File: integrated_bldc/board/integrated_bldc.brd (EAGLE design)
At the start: 26 x 23 mm, 68 parts, among them J2 PRG

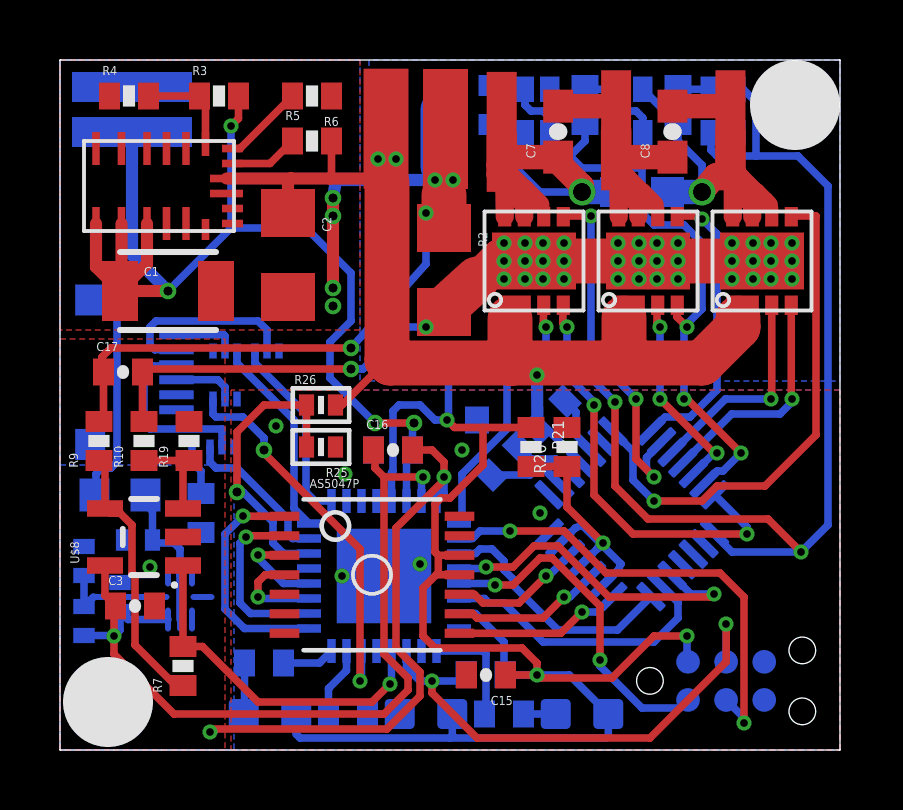
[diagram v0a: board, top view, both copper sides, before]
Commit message: Integrated BLDC is clean from Bay Area Circuits DFM check.
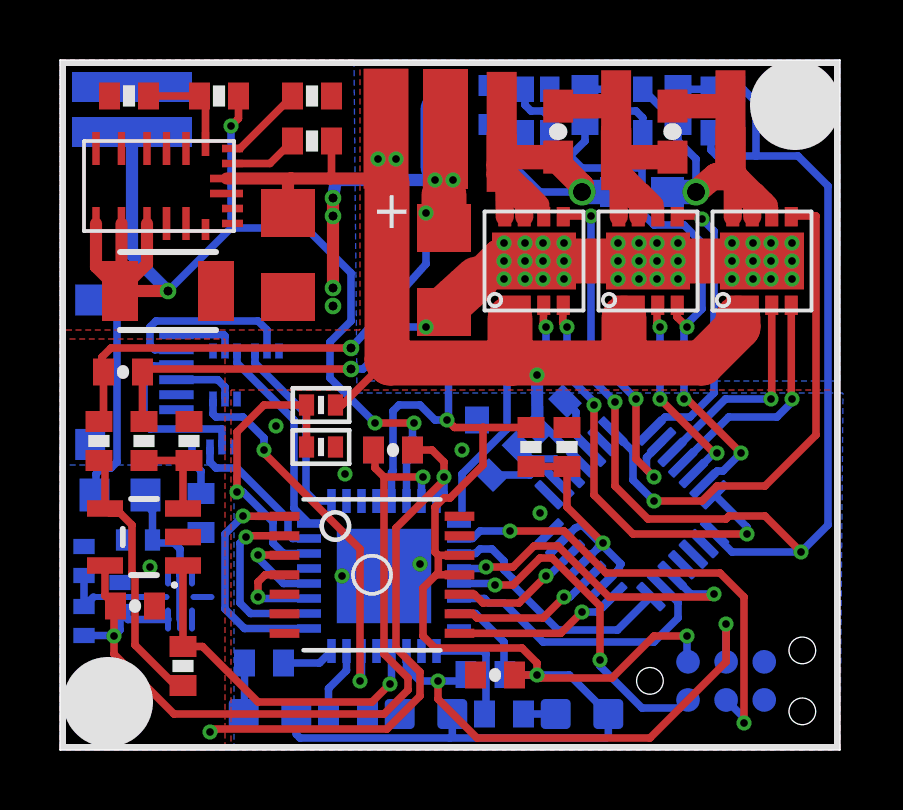
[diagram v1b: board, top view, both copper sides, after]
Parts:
- R14, R15, R8: value 220 -> 220R
- R2: value 0.01 -> 0R01
- moved C15 0.30 mm to (14.5, 2.50)
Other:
- board text added: "+"
- board text added: "-"
- board text added: "RX"
- board text added: "SCL"
- board text added: "SDA"
- board text added: "TX"

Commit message: Finished Dev board layout. Added stop mask to vias. Corrected some component values based on part order.
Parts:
- added U$16: (no value), modular_robotics:INFO
- D12: value GREEN -> WHITE
- R26: value 40k -> 39k
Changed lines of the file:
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@@
 <setting verticaltext="up"/>
 </settings>
-<grid distance="0.1" unitdist="mm" unit="mm" style="dots" multiple="1" display="yes" altdistance="0.005" altunitdist="mm" altunit="mm"/>
+<grid distance="0.1" unitdist="mm" unit="mm" style="dots" multiple="5" display="yes" altdistance="0.005" altunitdist="mm" altunit="mm"/>
 <layers>
 <layer number="1" name="Top" color="4" fill="1" visible="no" active="yes"/>
@@
 <layer number="24" name="bOrigins" color="15" fill="1" visible="yes" active="yes"/>
 <layer number="25" name="tNames" color="7" fill="1" visible="no" active="yes"/>
-<layer number="26" name="bNames" color="7" fill="1" visible="no" active="yes"/>
+<layer number="26" name="bNames" color="7" fill="1" visible="yes" active="yes"/>
 <layer number="27" name="tValues" color="7" fill="1" visible="no" active="yes"/>
-<layer number="28" name="bValues" color="7" fill="1" visible="no" active="yes"/>
+<layer number="28" name="bValues" color="7" fill="1" visible="yes" active="yes"/>
 <layer number="29" name="tStop" color="7" fill="3" visible="no" active="yes"/>
 <layer number="30" name="bStop" color="7" fill="6" visible="yes" active="yes"/>
@@
 <layer number="50" name="dxf" color="7" fill="1" visible="no" active="no"/>
 <layer number="51" name="tDocu" color="7" fill="1" visible="no" active="yes"/>
-<layer number="52" name="bDocu" color="7" fill="1" visible="yes" active="yes"/>
+<layer number="52" name="bDocu" color="7" fill="1" visible="no" active="yes"/>
 <layer number="53" name="tGND_GNDA" color="7" fill="9" visible="no" active="no"/>
 <layer number="54" name="bGND_GNDA" color="1" fill="9" visible="no" active="no"/>
@@
 <param name="mlMinCreamFrame" value="0mil"/>
 <param name="mlMaxCreamFrame" value="0mil"/>
-<param name="mlViaStopLimit" value="25mil"/>
+<param name="mlViaStopLimit" value="5mil"/>
 <param name="srRoundness" value="0"/>
 <param name="srMinRoundness" value="0mil"/>
@@
 </element>
 <element name="C4" library="SparkFun-Passives" package="0402-CAP" value="0.1uF" x="14.826" y="9.626" smashed="yes" rot="MR135">
-<attribute name="VALUE" x="12.75445625" y="9.1709" size="0.4064" layer="28" font="vector" ratio="25" rot="MR135"/>
+<attribute name="VALUE" x="13.15445625" y="9.3709" size="0.4064" layer="28" font="vector" ratio="25" rot="MR135"/>
 </element>
 <element name="C5" library="SparkFun-Passives" package="0402-CAP" value="0.1uF" x="16.374" y="11.172" smashed="yes" rot="MR315">
@@
 <element name="D7" library="SparkFun-LED" package="LED-0603" value="BLUE" x="12.2" y="1.2" smashed="yes" rot="MR270">
 <attribute name="PROD_ID" value="DIO-08575" x="12.2" y="1.2" size="1.778" layer="28" rot="MR270" display="off"/>
-<attribute name="VALUE" x="12.816" y="0.1205" size="0.4064" layer="28" font="vector" ratio="25" rot="MR0"/>
+<attribute name="VALUE" x="12.916" y="0.2205" size="0.4064" layer="28" font="vector" ratio="25" rot="MR0"/>
 </element>
 <element name="D11" library="SparkFun-LED" package="LED-0603" value="GREEN" x="7" y="1.2" smashed="yes" rot="MR270">
 <attribute name="PROD_ID" value="DIO-00821" x="7" y="1.2" size="1.778" layer="28" rot="MR270" display="off"/>
-<attribute name="VALUE" x="7.816" y="0.1205" size="0.4064" layer="28" font="vector" ratio="25" rot="MR0"/>
-</element>
-<element name="D12" library="SparkFun-LED" package="LED-0603" value="GREEN" x="17.4" y="1.2" smashed="yes" rot="MR270">
+<attribute name="VALUE" x="5.416" y="1.4205" size="0.4064" layer="28" font="vector" ratio="25" rot="MR0"/>
+</element>
+<element name="D12" library="SparkFun-LED" package="LED-0603" value="WHITE" x="17.4" y="1.2" smashed="yes" rot="MR270">
 <attribute name="PROD_ID" value="DIO-00821" x="17.4" y="1.2" size="1.778" layer="28" rot="MR270" display="off"/>
-<attribute name="VALUE" x="18.216" y="0.1205" size="0.4064" layer="28" font="vector" ratio="25" rot="MR0"/>
+<attribute name="VALUE" x="18.316" y="2.0205" size="0.4064" layer="28" font="vector" ratio="25" rot="MR0"/>
 </element>
 <element name="R8" library="SparkFun-Passives" package="0402-RES" value="220R" x="9.6" y="1.2" smashed="yes" rot="MR0">
-<attribute name="VALUE" x="10.1795" y="0.157" size="0.4064" layer="28" font="vector" ratio="25" rot="MR0"/>
+<attribute name="VALUE" x="9.5795" y="1.957" size="0.4064" layer="28" font="vector" ratio="25" rot="MR0"/>
 </element>
 <element name="R14" library="SparkFun-Passives" package="0402-RES" value="220R" x="6.8" y="2.9" smashed="yes" rot="MR180">
@@
 </element>
 <element name="R15" library="SparkFun-Passives" package="0402-RES" value="220R" x="14.8" y="1.2" smashed="yes" rot="MR0">
-<attribute name="VALUE" x="15.4795" y="0.157" size="0.4064" layer="28" font="vector" ratio="25" rot="MR0"/>
+<attribute name="VALUE" x="15.4795" y="0.257" size="0.4064" layer="28" font="vector" ratio="25" rot="MR0"/>
 </element>
 <element name="C7" library="SparkFun-Passives" package="0603-CAP" value="1nF" x="16.606" y="20.612" smashed="yes" rot="R90">
@@
 <element name="VOUT+" library="dhaldane" package="SMD_MOT_PAD" value="A" x="2.6" y="20.6" smashed="yes" rot="MR0"/>
 <element name="C11" library="SparkFun-Passives" package="0402-CAP" value="0.1uF" x="11.1" y="10" smashed="yes" rot="MR0">
-<attribute name="VALUE" x="10.1205" y="11.143" size="0.4064" layer="28" font="vector" ratio="25" rot="MR180"/>
+<attribute name="VALUE" x="8.1205" y="10.343" size="0.4064" layer="28" font="vector" ratio="25" rot="MR180"/>
 </element>
 <element name="SJ1" library="modular_robotics" package="SJ_TINY" value="SCL" x="5.5" y="11.7" smashed="yes" rot="MR90"/>
@@
 <element name="U$1" library="modular_robotics" package="MLPQ-UT8" value="SC560C" x="4" y="5.1" smashed="yes" rot="MR90"/>
 <element name="R13" library="biomimetic" package="0402-RES" value="20k" x="0.8" y="4.3" smashed="yes" rot="MR270">
-<attribute name="VALUE" x="1.4205" y="3.843" size="0.4064" layer="28" font="vector" ratio="25" rot="MR180"/>
+<attribute name="VALUE" x="1.7205" y="3.443" size="0.4064" layer="28" font="vector" ratio="25" rot="MR180"/>
 </element>
 <element name="R16" library="biomimetic" package="0402-RES" value="10k" x="0.8" y="6.3" smashed="yes" rot="MR270">
@@
 <attribute name="VALUE" x="7.5795" y="11.843" size="0.4064" layer="27" font="vector" ratio="25" rot="R180"/>
 </element>
-<element name="R26" library="biomimetic" package="0402-RES" value="40k" x="8.7" y="11.5" smashed="yes">
+<element name="R26" library="biomimetic" package="0402-RES" value="39k" x="8.7" y="11.5" smashed="yes">
 <attribute name="VALUE" x="8.8795" y="9.343" size="0.4064" layer="27" font="vector" ratio="25" rot="R180"/>
 </element>
@@
 <element name="R21" library="SparkFun-Passives" package="0402-RES" value="10k" x="15.7" y="10.1" smashed="yes" rot="R270">
 <attribute name="VALUE" x="15.643" y="7.9205" size="0.4064" layer="27" font="vector" ratio="25" rot="R90"/>
+</element>
+<element name="U$16" library="modular_robotics" package="INFO" value="" x="14.3" y="14.1" smashed="yes" rot="MR0">
+<attribute name="AUTHOR" value="D. Haldane, A. Buchan" x="16.3" y="18.2" size="0.8128" layer="22" font="vector" ratio="20" rot="MR0"/>
+<attribute name="DATE" value="Oct. 4, 2016" x="13.8" y="15.3" size="0.8128" layer="22" font="vector" ratio="20" rot="MR0"/>
+<attribute name="DESIGN" value="Integrated BLDC Dev" x="13.9" y="16.3" size="0.8128" layer="22" font="vector" ratio="20" rot="MR0"/>
+<attribute name="ORGANIZATION" value="Biomimetic Millisystems Lab" x="18.9" y="17.2" size="0.8128" layer="22" font="vector" ratio="20" rot="MR0"/>
+<attribute name="REVISION" value="r0.1" x="12.3" y="14.5" size="0.8128" layer="22" font="vector" ratio="20" rot="MR0"/>
 </element>
 </elements>
@@
 <wire x1="10.05" y1="3.3" x2="10.05" y2="2.35" width="0.254" layer="16"/>
 <wire x1="10.05" y1="2.35" x2="10" y2="2.3" width="0.254" layer="16"/>
-<via x="10" y="2.3" extent="1-16" drill="0.254"/>
+<via x="10" y="2.3" extent="1-16" drill="0.254" alwaysstop="yes"/>
 <via x="6.8" y="10" extent="1-16" drill="0.254"/>
 <wire x1="10" y1="6.7" x2="10" y2="2.3" width="0.254" layer="1"/>

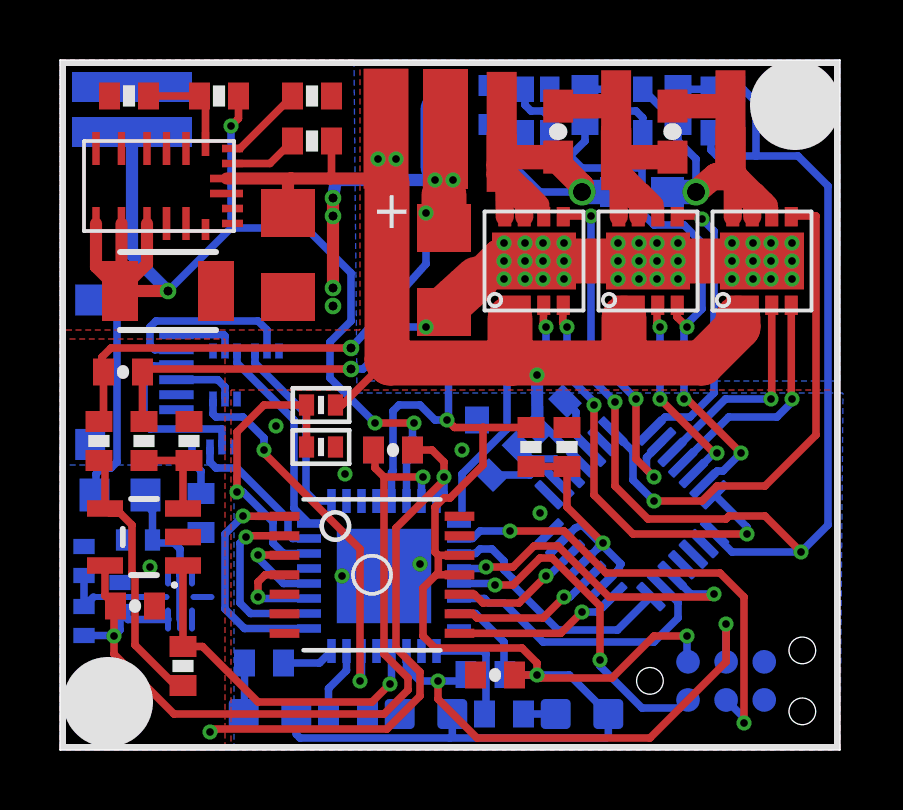
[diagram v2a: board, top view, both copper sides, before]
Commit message: Fixed spacing on DC-DC converter, updated all polygons to 0.15mm isolate for good measure.
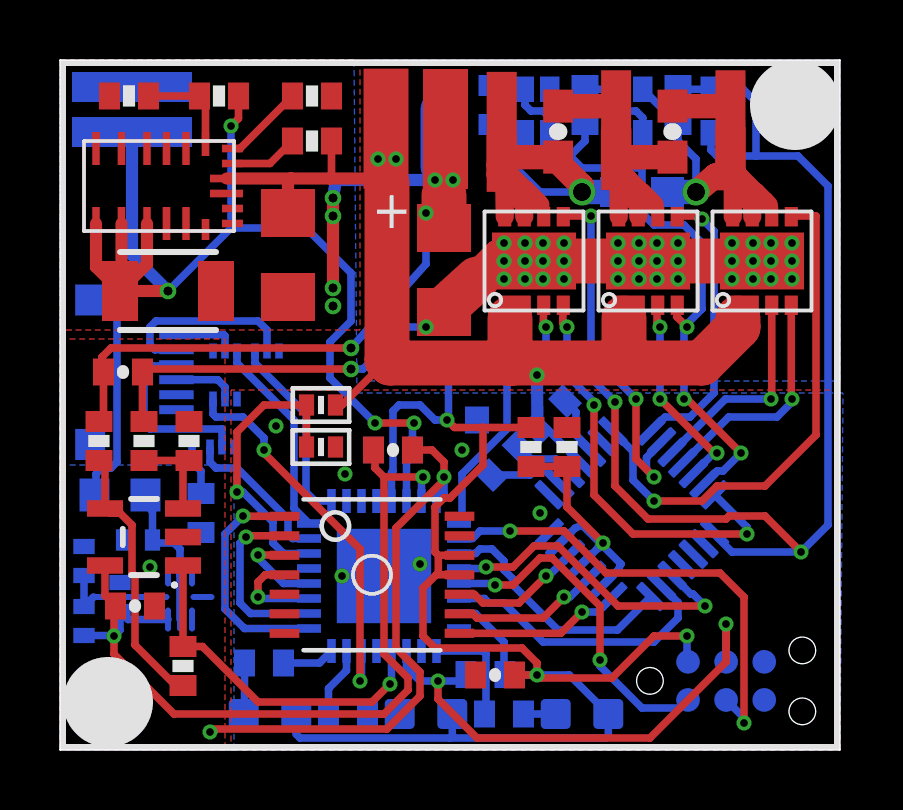
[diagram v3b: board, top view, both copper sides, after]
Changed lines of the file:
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@@
 <?xml version="1.0" encoding="utf-8"?>
 <!DOCTYPE eagle SYSTEM "eagle.dtd">
-<eagle version="6.6.0">
+<eagle version="6.5.0">
 <drawing>
 <settings>
@@
 <layer number="20" name="Dimension" color="15" fill="1" visible="yes" active="yes"/>
 <layer number="21" name="tPlace" color="7" fill="1" visible="no" active="yes"/>
-<layer number="22" name="bPlace" color="7" fill="1" visible="yes" active="yes"/>
+<layer number="22" name="bPlace" color="7" fill="1" visible="no" active="yes"/>
 <layer number="23" name="tOrigins" color="15" fill="1" visible="no" active="yes"/>
-<layer number="24" name="bOrigins" color="15" fill="1" visible="yes" active="yes"/>
+<layer number="24" name="bOrigins" color="15" fill="1" visible="no" active="yes"/>
 <layer number="25" name="tNames" color="7" fill="1" visible="no" active="yes"/>
-<layer number="26" name="bNames" color="7" fill="1" visible="yes" active="yes"/>
+<layer number="26" name="bNames" color="7" fill="1" visible="no" active="yes"/>
 <layer number="27" name="tValues" color="7" fill="1" visible="no" active="yes"/>
-<layer number="28" name="bValues" color="7" fill="1" visible="yes" active="yes"/>
+<layer number="28" name="bValues" color="7" fill="1" visible="no" active="yes"/>
 <layer number="29" name="tStop" color="7" fill="3" visible="no" active="yes"/>
-<layer number="30" name="bStop" color="7" fill="6" visible="yes" active="yes"/>
+<layer number="30" name="bStop" color="7" fill="6" visible="no" active="yes"/>
 <layer number="31" name="tCream" color="7" fill="4" visible="no" active="yes"/>
 <layer number="32" name="bCream" color="7" fill="5" visible="no" active="yes"/>
@@
 <layer number="38" name="bTest" color="7" fill="1" visible="no" active="yes"/>
 <layer number="39" name="tKeepout" color="4" fill="11" visible="no" active="yes"/>
-<layer number="40" name="bKeepout" color="1" fill="11" visible="yes" active="yes"/>
+<layer number="40" name="bKeepout" color="1" fill="11" visible="no" active="yes"/>
 <layer number="41" name="tRestrict" color="4" fill="10" visible="no" active="yes"/>
 <layer number="42" name="bRestrict" color="1" fill="10" visible="no" active="yes"/>
@@
 <layer number="46" name="Milling" color="3" fill="1" visible="no" active="yes"/>
 <layer number="47" name="Measures" color="7" fill="1" visible="no" active="yes"/>
-<layer number="48" name="Document" color="7" fill="1" visible="yes" active="yes"/>
+<layer number="48" name="Document" color="7" fill="1" visible="no" active="yes"/>
 <layer number="49" name="Reference" color="7" fill="1" visible="no" active="yes"/>
 <layer number="50" name="dxf" color="7" fill="1" visible="no" active="no"/>
@@
 <via x="12.5" y="19" extent="1-16" drill="0.254"/>
 <via x="13.1" y="19" extent="1-16" drill="0.254"/>
-<polygon width="0.22" layer="16" isolate="0.14" orphans="yes" rank="2">
+<polygon width="0.22" layer="16" isolate="0.15" orphans="yes" rank="2">
 <vertex x="0" y="0"/>
 <vertex x="26" y="0"/>
@@
 <wire x1="12.2" y1="16.2" x2="9.7" y2="13.4" width="0.254" layer="16"/>
 <via x="9.7" y="13.4" extent="1-16" drill="0.3"/>
-<polygon width="0.254" layer="1">
+<polygon width="0.254" layer="1" isolate="0.15">
 <vertex x="0" y="23"/>
 <vertex x="10" y="23"/>
@@
 <contactref element="U$3" pad="12"/>
 <wire x1="20.405503125" y1="5.8213875" x2="21.026890625" y2="5.2" width="0.254" layer="16"/>
-<wire x1="21.026890625" y1="5.2" x2="21.8" y2="5.2" width="0.254" layer="16"/>
 <via x="14.2" y="6.1" extent="1-16" drill="0.254"/>
 <wire x1="13.3" y1="6.05" x2="14.15" y2="6.05" width="0.254" layer="16"/>
 <wire x1="14.15" y1="6.05" x2="14.2" y2="6.1" width="0.254" layer="16"/>
-<via x="21.8" y="5.2" extent="1-16" drill="0.254"/>
+<via x="21.5" y="4.8" extent="1-16" drill="0.254"/>
 <wire x1="14.2" y1="6.1" x2="15.1" y2="6.1" width="0.254" layer="1"/>
 <wire x1="15.1" y1="6.1" x2="15.8" y2="6.8" width="0.254" layer="1"/>
 <wire x1="15.8" y1="6.8" x2="16.6" y2="6.8" width="0.254" layer="1"/>
-<wire x1="16.6" y1="6.8" x2="18.3" y2="5.1" width="0.254" layer="1"/>
-<wire x1="18.3" y1="5.1" x2="21.7" y2="5.1" width="0.254" layer="1"/>
-<wire x1="21.7" y1="5.1" x2="21.8" y2="5.2" width="0.254" layer="1"/>
+<wire x1="16.6" y1="6.8" x2="18.6" y2="4.8" width="0.254" layer="1"/>
+<wire x1="21.026890625" y1="5.2" x2="21.1" y2="5.2" width="0.254" layer="16"/>
+<wire x1="21.1" y1="5.2" x2="21.5" y2="4.8" width="0.254" layer="16"/>
+<wire x1="18.6" y1="4.8" x2="21.5" y2="4.8" width="0.254" layer="1"/>
 </signal>
 <signal name="EN">
@@
 <wire x1="12.8" y1="8.55" x2="12.8" y2="9.1" width="0.254" layer="16"/>
 <wire x1="12.4" y1="10" x2="12.8" y2="9.6" width="0.254" layer="1"/>
-<polygon width="0.254" layer="1" rank="2">
+<polygon width="0.254" layer="1" isolate="0.15" orphans="yes" rank="2">
 <vertex x="0" y="0"/>
 <vertex x="0" y="13.7"/>
@@
 <wire x1="13.9" y1="15.8" x2="14.6" y2="16.5" width="1.016" layer="1"/>
 <wire x1="14.6" y1="16.5" x2="15.576" y2="16.5" width="1.016" layer="1"/>
-<polygon width="0.254" layer="16" orphans="yes" rank="2">
+<polygon width="0.254" layer="16" isolate="0.15" orphans="yes" rank="2">
 <vertex x="10.3" y="12.3"/>
 <vertex x="26" y="12.3"/>
